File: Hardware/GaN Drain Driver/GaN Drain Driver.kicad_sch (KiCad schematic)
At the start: 36 parts, among them J1 SMA-J-P-H-ST-EM1, J2 Conn_01x02_Socket, J3 Conn_01x02_Socket, Q1 IRFS4321, Q2 IRFS4321, U1 LM317_SOT-223, U2 IRS2008S, U3 LM393

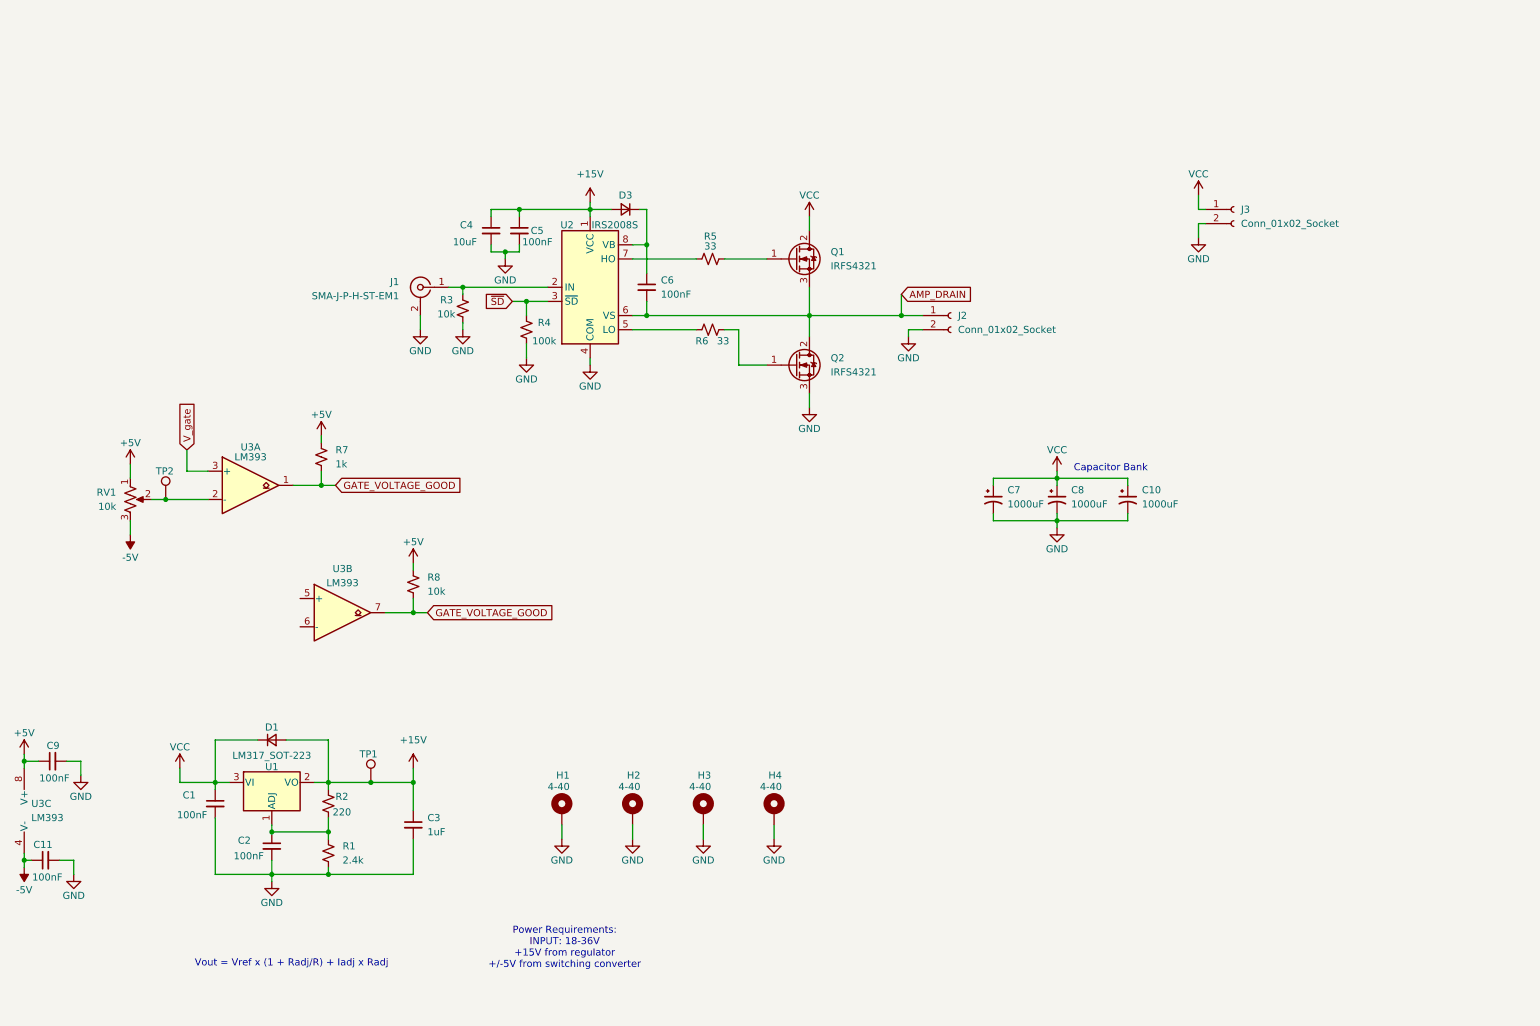
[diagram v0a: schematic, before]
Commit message: Updating GaN driver
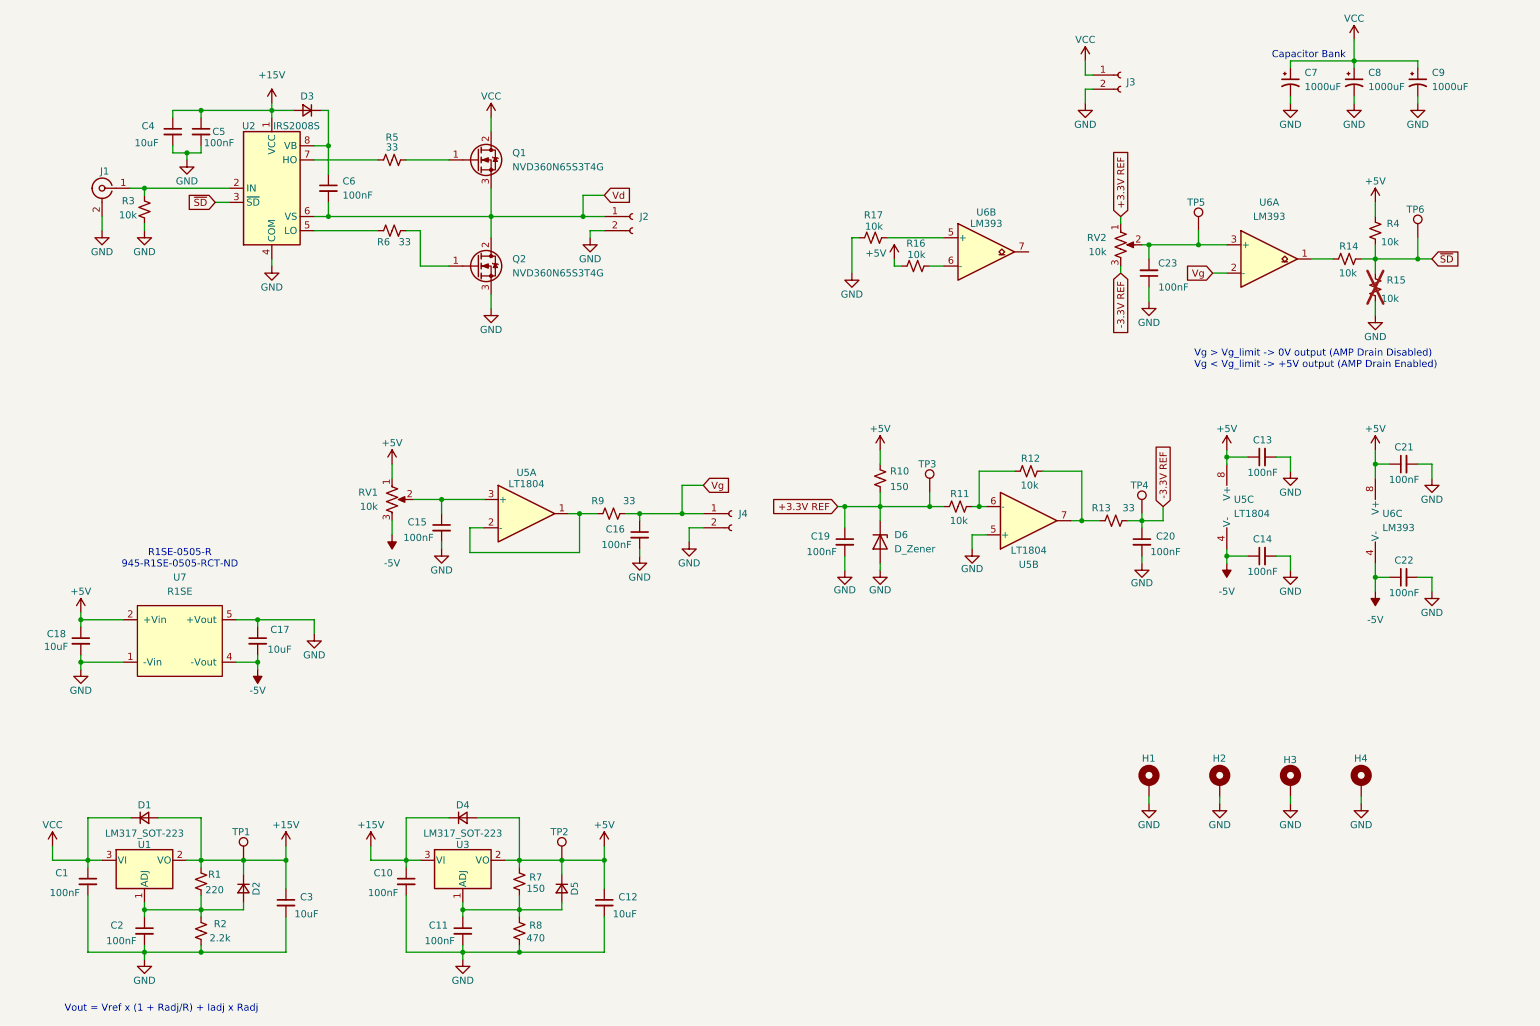
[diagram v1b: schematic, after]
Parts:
- removed C9: 100nF, Capacitor_SMD:C_0805_2012Metric, symbol Device:C_Small
- removed U3: LM393, symbol Comparator:LM393
- added C10, C13, C14, C15, C16, C19, C20, C21, C22, C23: 100nF, Capacitor_SMD:C_0805_2012Metric, symbol Device:C_Small
- added C12, C17, C18: 10uF, Capacitor_SMD:C_0805_2012Metric, symbol Device:C_Small
- added D2, D4, D5: 1N5819HW-7-F, Diode_SMD:D_SOD-123, symbol Device:D_Small
- added D6: D_Zener, Diode_SMD:D_SOD-123, symbol Device:D_Zener
- added J4: Conn_01x02_Socket, Connector_PinSocket_2.54mm:PinSocket_1x02_P2.54mm_Vertical, symbol Connector:Conn_01x02_Socket
- added R10: 150, Resistor_SMD:R_0805_2012Metric, symbol Device:R_Small_US
- added R11, R12, R14, R15, R16, R17: 10k, Resistor_SMD:R_0805_2012Metric, symbol Device:R_Small_US
- added R13, R9: 33, Resistor_SMD:R_0805_2012Metric, symbol Device:R_Small_US
- added RV2: 10k, Resistor_SMD:R_0805_2012Metric, symbol Device:R_Potentiometer_US
- added TP3, TP4, TP5, TP6: TestPoint, TestPoint:TestPoint_Pad_D1.0mm, symbol Connector:TestPoint
- added U3: LM317_SOT-223, Package_TO_SOT_SMD:SOT-223-3_TabPin2, symbol Regulator_Linear:LM317_SOT-223
- added U5: LT1804, Package_SO:SOIC-8_3.9x4.9mm_P1.27mm, symbol Amplifier_Operational:LMV358
- added U6: LM393, Package_SO:SOIC-8_3.9x4.9mm_P1.27mm, symbol Comparator:LM393
- added U7: R1SE, _tim-DC-DC:R1SE_SMD5_12.75X10.7X6.7_SINGLE_RCP, symbol _tim-DC_DC:R1SE
- C3: value 1uF -> 10uF
- Q1, Q2: value IRFS4321 -> NVD360N65S3T4G; footprint Package_TO_SOT_SMD:TO-263-2 -> Package_TO_SOT_SMD:TO-252-2; Digikey IRFS4321TRLPBFCT-ND -> 488-NVD360N65S3T4GCT-ND
- R2: renamed from R1; value 2.4k -> 2.2k
- R4: value 100k -> 10k
- R7: value 1k -> 150; footprint (none) -> Resistor_SMD:R_0805_2012Metric
- R8: value 10k -> 470; footprint (none) -> Resistor_SMD:R_0805_2012Metric
- RV1: footprint (none) -> Resistor_SMD:R_0805_2012Metric
- TP2: footprint (none) -> TestPoint:TestPoint_Pad_D1.0mm
- U1: Digikey (none) -> 296-12631-1-ND
- U2: Digikey (none) -> IRS2008STRPBFCT-ND
- renumbered C10 to C9, R2 to R1
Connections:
- net +15V: now also C10.1, D2.1 (K), D4.1 (K), U3.3 (VI)
- net +5V: now also R4.1, TP2.1, C12.1, C13.1, C18.1, C21.1, D4.2 (A), D5.1 (K), R10.1, R16.1, U3.2 (VO), U5.8 (V+), U6.8 (V+), U7.2 (+Vin); no longer R8.1
- net -5V: now also C14.1, C17.2, C22.1, U5.4 (V-), U6.4 (V-), U7.4 (-Vout); no longer C11.1
- net GND: now also R8.2, C10.2, C12.2, C13.2, C14.2, C15.2, C16.2, C17.1, C18.2, C19.2, C20.2, C21.2, C22.2, C23.1, D6.2 (A), J4.2 (Pin_2), R15.2, R17.1, U5.5 (+), U7.1 (-Vin), U7.5 (+Vout); no longer R4.2
- net ~{SD}: now also R4.2, R14.2, R15.1, TP6.1; no longer R4.1
- net at RV1.2: now also C15.1, U5.3 (+); no longer TP2.1
- net at C2.1, R1.2, R2.1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: now also D2.2 (A)
- net AMP_DRAIN renamed Vd
- net GATE_VOLTAGE_GOOD: no longer names the net of R7.2
- net GATE_VOLTAGE_GOOD: now also C11.1, R8.1, D5.2 (A), U3.1 (ADJ); no longer R8.2
- new net: R17.2, U6.5 (+)
- new net: R9.1, U5.1, U5.2 (-)
- new net: R12.2, R13.1, U5.7
- new net: R14.1, U6.1
- new net: C23.2, RV2.2, TP5.1, U6.3 (+)
- new net: R11.2, R12.1, U5.6 (-)
- new net: R16.2, U6.6 (-)
- new net +3.3V REF: C19.1, D6.1 (K), R10.2, R11.1, RV2.1, TP3.1
- new net -3.3V REF: C20.1, R13.2, RV2.3, TP4.1
- new net Vg: C16.1, J4.1 (Pin_1), R9.2, U6.2 (-)
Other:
- note added: "R1SE-0505-R 945-R1SE-0505-RCT-ND"
- note added: "Vg > Vg_limit -> 0V output (AMP Drain Disabled) Vg < Vg_limit -> +5V output (AMP Drain Enabled)"
- note removed: "Power Requirements: INPUT: 18-36V +15V from regulator +/-5V from switching converter"
- moved on the sheet: C1, C2, C4, C5, C6, C7, C8, C9, D1, D3, H1, H2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

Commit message: Updating schematic
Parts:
- removed R16: 10k, Resistor_SMD:R_0805_2012Metric, symbol Device:R_Small_US
- added C24: 10uF, Capacitor_SMD:C_0805_2012Metric, symbol Device:C_Small
- added R18, R19: 10k, Resistor_SMD:R_0805_2012Metric, symbol Device:R_Small_US
- D6: value D_Zener -> 3.3V; Digikey (none) -> DDZ9684-7DICT-ND
- R17: value 10k -> 100k
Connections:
- net +3.3V REF: now also R17.1
- net +5V: now also R18.2
- net GND: now also C24.2, R19.1; no longer R17.1
- net at R17.2, U6.5 (+): now also C24.1
- net COMP_OUT: now reaches R14.1, U6.1
- net COMP_OUT: now also U6.7
- net at U6.6 (-): now also R18.1, R19.2
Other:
- note added: "Time Delay Circuit"
- moved on the sheet: R17, U6B

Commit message: working on board layout
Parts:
- removed C4: 10uF, Capacitor_SMD:C_0805_2012Metric, symbol Device:C_Small
- removed C7: 1000uF, Capacitor_THT:CP_Radial_D13.0mm_P5.00mm, symbol Device:C_Polarized_Small_US
- added TP7: TestPoint, TestPoint:TestPoint_Pad_D1.0mm, symbol Connector:TestPoint
- J2: footprint Connector_PinSocket_2.54mm:PinSocket_1x02_P2.54mm_Vertical -> Connector_Molex:Molex_KK-254_AE-6410-02A_1x02_P2.54mm_Vertical
- J3: renamed from J4; footprint Connector_PinSocket_2.54mm:PinSocket_1x02_P2.54mm_Vertical -> Connector_Molex:Molex_KK-254_AE-6410-02A_1x02_P2.54mm_Vertical
- J4: renamed from J3; footprint Connector_PinSocket_2.54mm:PinSocket_1x02_P2.54mm_Vertical -> Connector_Molex:Molex_KK-254_AE-6410-02A_1x02_P2.54mm_Vertical
- RV1, RV2: footprint Resistor_SMD:R_0805_2012Metric -> Potentiometer_THT:Potentiometer_Bourns_3296W_Vertical
- renumbered C18 to C1, C15 to C10, C16 to C13, C24 to C14, C19 to C15, C20 to C16, C23 to C17, C13 to C18, C14 to C19, C1 to C2, C8 to C21, C21 to C22, C22 to C23, C9 to C24, C2 to C3, C17 to C6, C3 to C7, C6 to C8, C10 to C9, R3 to R1, R18 to R10, R19 to R11, R10 to R12, R11 to R13, R12 to R14, R13 to R15, R14 to R16, R4 to R17, R15 to R18, R1 to R2, R2 to R3, R5 to R4, R6 to R5, R7 to R6, R8 to R7, R9 to R8, R17 to R9, U7 to U2, U2 to U3, U3 to U4
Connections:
- net -5V: now also TP7.1
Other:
- moved on the sheet: C5

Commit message: Working on Board Layout
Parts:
- added C20, C4: 1000uF, Capacitor_THT:CP_Radial_D13.0mm_P5.00mm, symbol Device:C_Polarized_Small_US
- R18: value 10k -> 10M
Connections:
- net +3.3V REF: no longer R9.1
- net +5V: now also R9.1
- net GND: now also C20.2, C4.2
- net VCC: now also C20.1, C4.1

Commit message: Updating board
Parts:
- added TP8, TP9: TestPoint, TestPoint:TestPoint_Pad_D1.0mm, symbol Connector:TestPoint
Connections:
- net +3.3V REF: now also RV1.1
- net +5V: no longer RV1.1
- net -3.3V REF: now also RV1.3
- net -5V: no longer RV1.3
- net Vg: now also TP8.1
- net at C10.1, RV1.2, U5.3 (+): now also TP9.1
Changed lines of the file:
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@@
 	)
 	(junction
+		(at 132.08 104.14)
+		(diameter 0)
+		(color 0 0 0 0)
+	)
+	(junction
 		(at 260.35 115.57)
 		(diameter 0)
@@
 	(wire
 		(pts
+			(xy 132.08 101.6) (xy 132.08 104.14)
+		)
+		(stroke
+			(width 0)
+			(type default)
+		)
+	)
+	(wire
+		(pts
 			(xy 180.34 100.33) (xy 180.34 102.87)
 		)
@@
 	(wire
 		(pts
-			(xy 135.89 104.14) (xy 128.27 104.14)
+			(xy 135.89 104.14) (xy 132.08 104.14)
 		)
 		(stroke
@@
 	(wire
 		(pts
+			(xy 92.71 100.33) (xy 92.71 101.6)
+		)
+		(stroke
+			(width 0)
+			(type default)
+		)
+	)
+	(wire
+		(pts
 			(xy 248.92 58.42) (xy 250.19 58.42)
 		)
@@
 	(wire
 		(pts
+			(xy 132.08 104.14) (xy 128.27 104.14)
+		)
+		(stroke
+			(width 0)
+			(type default)
+		)
+	)
+	(wire
+		(pts
 			(xy 62.23 58.42) (xy 62.23 59.69)
 		)
@@
 		)
 	)
+	(global_label "-3.3V REF"
+		(shape input)
+		(at 83.82 107.95 270)
+		(fields_autoplaced yes)
+		(effects
+			(font
+				(size 1.27 1.27)
+			)
+			(justify right)
+		)
+		(property "Intersheetrefs" "${INTERSHEET_REFS}"
+			(at 83.82 121.0952 90)
+			(effects
+				(font
+					(size 1.27 1.27)
+				)
+				(justify right)
+				(hide yes)
+			)
+		)
+	)
+	(global_label "+3.3V REF"
+		(shape input)
+		(at 83.82 95.25 90)
+		(fields_autoplaced yes)
+		(effects
+			(font
+				(size 1.27 1.27)
+			)
+			(justify left)
+		)
+		(property "Intersheetrefs" "${INTERSHEET_REFS}"
+			(at 83.82 82.1048 90)
+			(effects
+				(font
+					(size 1.27 1.27)
+				)
+				(justify left)
+				(hide yes)
+			)
+		)
+	)
 	(global_label "+3.3V REF"
 		(shape input)
@@
 	)
 	(symbol
+		(lib_id "Connector:TestPoint")
+		(at 92.71 100.33 0)
+		(unit 1)
+		(exclude_from_sim no)
+		(in_bom yes)
+		(on_board yes)
+		(dnp no)
+		(property "Reference" "TP9"
+			(at 90.678 95.25 0)
+			(effects
+				(font
+					(size 1.27 1.27)
+				)
+				(justify left)
+			)
+		)
+		(property "Value" "TestPoint"
+			(at 89.408 98.298 0)
+			(effects
+				(font
+					(size 1.27 1.27)
+				)
+				(justify left)
+				(hide yes)
+			)
+		)
+		(property "Footprint" "TestPoint:TestPoint_Pad_D1.0mm"
+			(at 97.79 100.33 0)
+			(effects
+				(font
+					(size 1.27 1.27)
+				)
+				(hide yes)
+			)
+		)
+		(property "Datasheet" "~"
+			(at 97.79 100.33 0)
+			(effects
+				(font
+					(size 1.27 1.27)
+				)
+				(hide yes)
+			)
+		)
+		(property "Description" "test point"
+			(at 92.71 100.33 0)
+			(effects
+				(font
+					(size 1.27 1.27)
+				)
+				(hide yes)
+			)
+		)
+		(pin "1"
+		)
+		(instances
+			(project "GaN Drain Driver"
+				(path "/25bb5703-5946-409a-bc14-ea92dd4cb5e5"
+					(reference "TP9")
+					(unit 1)
+				)
+			)
+		)
+	)
+	(symbol
 		(lib_id "power:GND")
 		(at 165.1 114.3 0)
@@
 	)
 	(symbol
-		(lib_id "power:-5V")
-		(at 83.82 107.95 180)
-		(unit 1)
-		(exclude_from_sim no)
-		(in_bom yes)
-		(on_board yes)
-		(dnp no)
-		(fields_autoplaced yes)
-		(property "Reference" "#PWR015"
-			(at 83.82 104.14 0)
-			(effects
-				(font
-					(size 1.27 1.27)
-				)
-				(hide yes)
-			)
-		)
-		(property "Value" "-5V"
-			(at 83.82 113.03 0)
-			(effects
-				(font
-					(size 1.27 1.27)
-				)
-			)
-		)
-		(property "Footprint" ""
-			(at 83.82 107.95 0)
-			(effects
-				(font
-					(size 1.27 1.27)
-				)
-				(hide yes)
-			)
-		)
-		(property "Datasheet" ""
-			(at 83.82 107.95 0)
-			(effects
-				(font
-					(size 1.27 1.27)
-				)
-				(hide yes)
-			)
-		)
-		(property "Description" "Power symbol creates a global label with name \"-5V\""
-			(at 83.82 107.95 0)
-			(effects
-				(font
-					(size 1.27 1.27)
-				)
-				(hide yes)
-			)
-		)
-		(pin "1"
-		)
-		(instances
-			(project "GaN Drain Driver"
-				(path "/25bb5703-5946-409a-bc14-ea92dd4cb5e5"
-					(reference "#PWR015")
-					(unit 1)
-				)
-			)
-		)
-	)
-	(symbol
 		(lib_id "Device:C_Small")
 		(at 240.03 93.98 90)
@@
 	)
 	(symbol
+		(lib_id "Connector:TestPoint")
+		(at 132.08 101.6 0)
+		(unit 1)
+		(exclude_from_sim no)
+		(in_bom yes)
+		(on_board yes)
+		(dnp no)
+		(property "Reference" "TP8"
+			(at 130.048 96.52 0)
+			(effects
+				(font
+					(size 1.27 1.27)
+				)
+				(justify left)
+			)
+		)
+		(property "Value" "TestPoint"
+			(at 128.778 99.568 0)
+			(effects
+				(font
+					(size 1.27 1.27)
+				)
+				(justify left)
+				(hide yes)
+			)
+		)
+		(property "Footprint" "TestPoint:TestPoint_Pad_D1.0mm"
+			(at 137.16 101.6 0)
+			(effects
+				(font
+					(size 1.27 1.27)
+				)
+				(hide yes)
+			)
+		)
+		(property "Datasheet" "~"
+			(at 137.16 101.6 0)
+			(effects
+				(font
+					(size 1.27 1.27)
+				)
+				(hide yes)
+			)
+		)
+		(property "Description" "test point"
+			(at 132.08 101.6 0)
+			(effects
+				(font
+					(size 1.27 1.27)
+				)
+				(hide yes)
+			)
+		)
+		(pin "1"
+		)
+		(instances
+			(project "GaN Drain Driver"
+				(path "/25bb5703-5946-409a-bc14-ea92dd4cb5e5"
+					(reference "TP8")
+					(unit 1)
+				)
+			)
+		)
+	)
+	(symbol
 		(lib_id "power:+5V")
 		(at 233.68 92.71 0)
@@
 					(unit 1)
 				)
-			)
-		)
-	)
-	(symbol
-		(lib_id "power:+5V")
-		(at 83.82 95.25 0)
-		(unit 1)
-		(exclude_from_sim no)
-		(in_bom yes)
-		(on_board yes)
-		(dnp no)
-		(property "Reference" "#PWR014"
-			(at 83.82 99.06 0)
-			(effects
-				(font
-					(size 1.27 1.27)
-				)
-				(hide yes)
-			)
-		)
-		(property "Value" "+5V"
-			(at 83.82 91.44 0)
-			(effects
-				(font
-					(size 1.27 1.27)
-				)
-			)
-		)
-		(property "Footprint" ""
-			(at 83.82 95.25 0)
-			(effects
-				(font
-					(size 1.27 1.27)
-				)
-				(hide yes)
-			)
-		)
-		(property "Datasheet" ""
-			(at 83.82 95.25 0)
-			(effects
-				(font
-					(size 1.27 1.27)
-				)
-				(hide yes)
-			)
-		)
-		(property "Description" "Power symbol creates a global label with name \"+5V\""
-			(at 83.82 95.25 0)
-			(effects
-				(font
-					(size 1.27 1.27)
-				)
-				(hide yes)
-			)
-		)
-		(pin "1"
-		)
-		(instances
-			(project "GaN Drain Driver"
-				(path "/25bb5703-5946-409a-bc14-ea92dd4cb5e5"
-					(reference "#PWR014")
-					(unit 1)
-				)

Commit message: Updating BOM
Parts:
- U2: Digikey (none) -> 945-R1SE-0505-RCT-ND
- U6: Digikey (none) -> 497-1593-1-ND
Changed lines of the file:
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@@
 			)
 		)
+		(property "Digikey" "497-1593-1-ND"
+			(at 262.89 105.41 0)
+			(effects
+				(font
+					(size 1.27 1.27)
+				)
+				(hide yes)
+			)
+		)
 		(pin "4"
 		)
@@
 			)
 		)
+		(property "Digikey" "945-R1SE-0505-RCT-ND"
+			(at 45.72 127 0)
+			(effects
+				(font
+					(size 1.27 1.27)
+				)
+				(hide yes)
+			)
+		)
 		(pin "2"
 		)
@@
 			)
 		)
+		(property "Digikey" "497-1593-1-ND"
+			(at 179.07 67.31 0)
+			(effects
+				(font
+					(size 1.27 1.27)
+				)
+				(hide yes)
+			)
+		)
 		(pin "4"
 		)
@@
 			(at 241.3 58.42 0)
 			(effects
+				(font
+					(size 1.27 1.27)
+				)
+				(hide yes)
+			)
+		)
+		(property "Digikey" "497-1593-1-ND"
+			(at 241.3 58.42 0)
+			(effects

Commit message: Updating BOM
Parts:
- H1, H2, H3, H4, TP1, TP2, TP3, TP4, TP5, TP6, TP8, TP9: now left out of the parts list
- J1: Digikey (none) -> SAM8857-ND
- J2, J3, J4: Digikey (none) -> WM4111-ND
- RV1, RV2: Digikey (none) -> 3296W-103LF-ND
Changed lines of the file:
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@@
 		(unit 1)
 		(exclude_from_sim no)
-		(in_bom yes)
+		(in_bom no)
 		(on_board yes)
 		(dnp no)
@@
 		(unit 1)
 		(exclude_from_sim no)
-		(in_bom yes)
+		(in_bom no)
 		(on_board yes)
 		(dnp no)
@@
 			)
 		)
+		(property "Digikey" "SAM8857-ND"
+			(at 31.75 45.72 0)
+			(effects
+				(font
+					(size 1.27 1.27)
+				)
+				(hide yes)
+			)
+		)
 		(pin "1"
 		)
@@
 			)
 		)
+		(property "Digikey" "3296W-103LF-ND"
+			(at 83.82 101.6 0)
+			(effects
+				(font
+					(size 1.27 1.27)
+				)
+				(hide yes)
+			)
+		)
 		(pin "2"
 		)
@@
 		(unit 1)
 		(exclude_from_sim no)
-		(in_bom yes)
+		(in_bom no)
 		(on_board yes)
 		(dnp no)
@@
 		(unit 1)
 		(exclude_from_sim no)
-		(in_bom yes)
+		(in_bom no)
 		(on_board yes)
 		(dnp no)
@@
 			)
 		)
+		(property "Digikey" "WM4111-ND"
+			(at 127 50.8 0)
+			(effects
+				(font
+					(size 1.27 1.27)
+				)
+				(hide yes)
+			)
+		)
 		(pin "2"
 		)
@@
 		(unit 1)
 		(exclude_from_sim no)
-		(in_bom yes)
+		(in_bom no)
 		(on_board yes)
 		(dnp no)
@@
 		(unit 1)
 		(exclude_from_sim no)
-		(in_bom yes)
+		(in_bom no)
 		(on_board yes)
 		(dnp no)
@@
 		(unit 1)
 		(exclude_from_sim no)
-		(in_bom yes)
+		(in_bom no)
 		(on_board yes)
 		(dnp no)
@@
 		(unit 1)
 		(exclude_from_sim no)
-		(in_bom yes)
+		(in_bom no)
 		(on_board yes)
 		(dnp no)
@@
 		(unit 1)
 		(exclude_from_sim no)
-		(in_bom yes)
+		(in_bom no)
 		(on_board yes)
 		(dnp no)
@@
 			)
 		)
+		(property "Digikey" "3296W-103LF-ND"
+			(at 214.63 55.88 0)
+			(effects
+				(font
+					(size 1.27 1.27)
+				)
+				(hide yes)
+			)
+		)
 		(pin "2"
 		)
@@
 			)
 		)
+		(property "Digikey" "WM4111-ND"
+			(at 214.63 25.4 0)
+			(effects
+				(font
+					(size 1.27 1.27)
+				)
+				(hide yes)
+			)
+		)
 		(pin "2"
 		)
@@
 		(unit 1)
 		(exclude_from_sim no)
-		(in_bom yes)
+		(in_bom no)
 		(on_board yes)
 		(dnp no)
@@
 		(unit 1)
 		(exclude_from_sim no)
-		(in_bom yes)
+		(in_bom no)
 		(on_board yes)
 		(dnp no)
@@
 		(unit 1)
 		(exclude_from_sim no)
-		(in_bom yes)
+		(in_bom no)
 		(on_board yes)
 		(dnp no)
@@
 			(at 144.78 104.14 0)
 			(effects
+				(font
+					(size 1.27 1.27)
+				)
+				(hide yes)
+			)
+		)
+		(property "Digikey" "WM4111-ND"
+			(at 144.78 104.14 0)
+			(effects

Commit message: Fixing issue with reference
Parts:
- removed D6: 3.3V, Diode_SMD:D_SOD-123, symbol Device:D_Zener
- removed R12: 150, Resistor_SMD:R_0805_2012Metric, symbol Device:R_Small_US
- added C13: 10uF, Capacitor_SMD:C_0805_2012Metric, symbol Device:C_Small
- added C15, C17: 100nF, Capacitor_SMD:C_0805_2012Metric, symbol Device:C_Small
- added U6: MAX6241, Package_SO:SOIC-8_3.9x4.9mm_P1.27mm, symbol Reference_Voltage:MAX6241
- renumbered C11 to C10, C12 to C11, C13 to C12, C15 to C16, C16 to C18, C17 to C19, C18 to C21, C19 to C22, C4 to C23, C21 to C24, C22 to C25, C23 to C26, C24 to C27, C5 to C4, C6 to C5, C7 to C6, C8 to C7, C9 to C8, C10 to C9, R13 to R12, R14 to R13, R15 to R14, R16 to R15, R17 to R16, R18 to R17, TP7 to TP2, TP9 to TP3, TP2 to TP4, TP8 to TP5, TP3 to TP6, TP4 to TP7, TP5 to TP8, TP6 to TP9, U6 to U7
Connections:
- net +15V: now also C15.2, U6.2 (IN)
- net GND: now also C13.2, C15.1, C17.2, U6.4 (GND)
- net +3.3V REF renamed +4.096V REF
- net +4.096V REF: now also C17.1, U6.6 (OUT)
- net -3.3V REF renamed -4.096V REF
- new net: C13.1, U6.3 (NR)
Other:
- moved on the sheet: C16
